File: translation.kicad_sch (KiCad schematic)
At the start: 9 parts, among them Q1 DMG1012UW-7, Q2 DMG1012UW-7, U4 FXLA108BQX

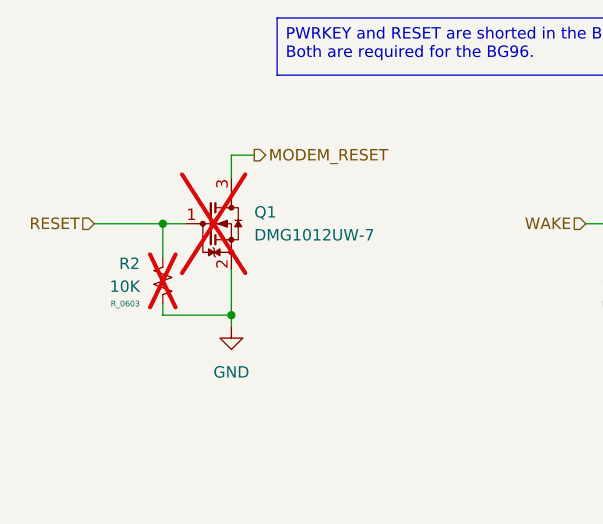
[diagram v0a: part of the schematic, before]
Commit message: Update export scripts
Change DNF options
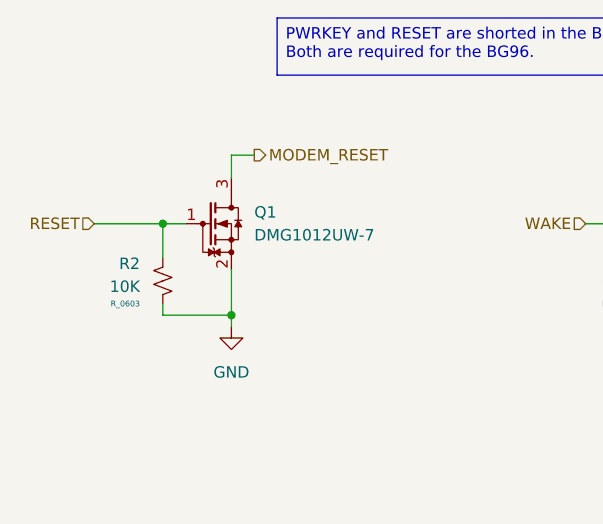
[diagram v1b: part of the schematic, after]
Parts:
- Q1, R2: now fitted
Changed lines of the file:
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@@
 	(title_block
 		(title "Winglet BG95")
-		(date "2025-06-05")
-		(rev "v1.1")
+		(date "2025-09-29")
+		(rev "v1.1b")
 		(company "TL Embedded")
 	)
@@
 		(in_bom yes)
 		(on_board yes)
-		(dnp yes)
+		(dnp no)
 		(property "Reference" "R2"
 			(at 71.12 51.435 0)
@@
 		(in_bom yes)
 		(on_board yes)
-		(dnp yes)
+		(dnp no)
 		(fields_autoplaced yes)
 		(property "Reference" "Q1"
